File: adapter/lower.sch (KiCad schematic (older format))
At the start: 13 parts, among them J1 MALE, J2 FEMALE, J3 STANDOFF, J4 STANDOFF, J5 STANDOFF, J6 USB_C_Receptacle_USB2.0, J7 DTR, U1 FT232RL

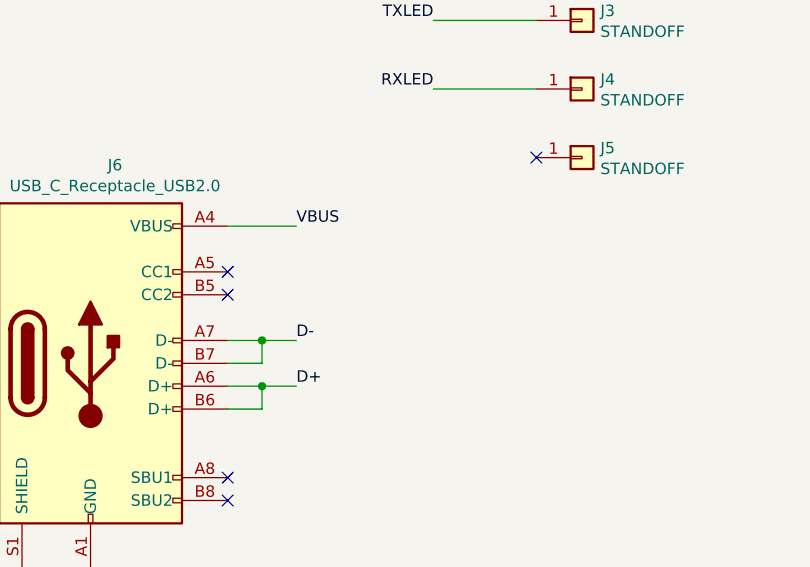
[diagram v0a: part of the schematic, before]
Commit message: Add 56k pullups to fake USB host signature
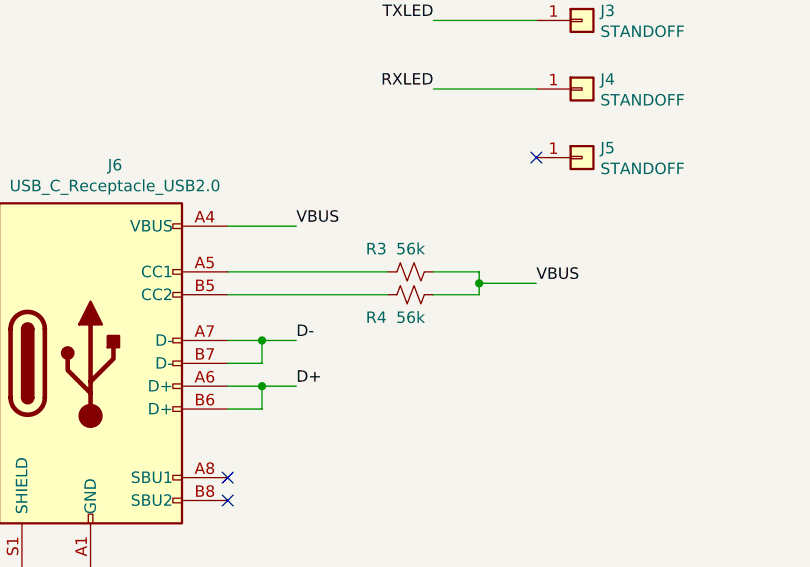
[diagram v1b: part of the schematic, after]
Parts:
- added R3, R4: 56k, symbol Device:R_Small_US
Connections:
- net VBUS: now also R3.1, R4.1
- net at J6.A5 (CC1): now also R3.2
- net at J6.B5 (CC2): now also R4.2
- no-connect marks 16 -> 14
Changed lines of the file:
@@
 	1    0    0    -1
 $EndComp
-NoConn ~ 2150 4100
-NoConn ~ 2150 4200
 NoConn ~ 2150 5000
 NoConn ~ 2150 5100
@@
 $EndComp
 $Comp
-L node:+5VB #PWR?
+L node:+5VB #PWR04
 U 1 1 5FBBDFD6
 P 2550 1100
-F 0 "#PWR?" H 2550 950 50  0001 C CNN
+F 0 "#PWR04" H 2550 950 50  0001 C CNN
 F 1 "+5VB" H 2565 1273 50  0000 C CNN
 F 2 "" H 2550 1100 50  0001 C CNN
@@
 	1200 2200 1200 2450
 $Comp
-L node:+5VB #PWR?
+L node:+5VB #PWR01
 U 1 1 5FBC099F
 P 1200 2200
-F 0 "#PWR?" H 1200 2050 50  0001 C CNN
+F 0 "#PWR01" H 1200 2050 50  0001 C CNN
 F 1 "+5VB" H 1215 2373 50  0000 C CNN
 F 2 "" H 1200 2200 50  0001 C CNN
@@
 $EndComp
 $Comp
-L node:+5VB #PWR?
+L node:+5VB #PWR09
 U 1 1 5FBC0B3A
 P 9000 2000
-F 0 "#PWR?" H 9000 1850 50  0001 C CNN
+F 0 "#PWR09" H 9000 1850 50  0001 C CNN
 F 1 "+5VB" H 9015 2173 50  0000 C CNN
 F 2 "" H 9000 2000 50  0001 C CNN
@@
 $EndComp
 $Comp
-L node:GNDB #PWR?
+L node:GNDB #PWR02
 U 1 1 5FBC113D
 P 1550 5600
-F 0 "#PWR?" H 1550 5350 50  0001 C CNN
+F 0 "#PWR02" H 1550 5350 50  0001 C CNN
 F 1 "GNDB" H 1555 5427 50  0000 C CNN
 F 2 "" H 1550 5600 50  0001 C CNN
@@
 $EndComp
 $Comp
-L node:GNDB #PWR?
+L node:GNDB #PWR03
 U 1 1 5FBC146F
 P 1650 2450
-F 0 "#PWR?" H 1650 2200 50  0001 C CNN
+F 0 "#PWR03" H 1650 2200 50  0001 C CNN
 F 1 "GNDB" H 1655 2277 50  0000 C CNN
 F 2 "" H 1650 2450 50  0001 C CNN
@@
 $EndComp
 $Comp
-L node:GNDB #PWR?
+L node:GNDB #PWR08
 U 1 1 5FBC158B
 P 7850 4900
-F 0 "#PWR?" H 7850 4650 50  0001 C CNN
+F 0 "#PWR08" H 7850 4650 50  0001 C CNN
 F 1 "GNDB" H 8050 4850 50  0000 C CNN
 F 2 "" H 7850 4900 50  0001 C CNN
@@
 $EndComp
 $Comp
-L node:GNDB #PWR?
+L node:GNDB #PWR010
 U 1 1 5FBC1AD4
 P 9000 2700
-F 0 "#PWR?" H 9000 2450 50  0001 C CNN
+F 0 "#PWR010" H 9000 2450 50  0001 C CNN
 F 1 "GNDB" H 9200 2650 50  0000 C CNN
 F 2 "" H 9000 2700 50  0001 C CNN
@@
 $EndComp
 $Comp
-L node:GNDB #PWR?
+L node:GNDB #PWR06
 U 1 1 5FBC1BF2
 P 6000 2650
-F 0 "#PWR?" H 6000 2400 50  0001 C CNN
+F 0 "#PWR06" H 6000 2400 50  0001 C CNN
 F 1 "GNDB" H 6200 2600 50  0000 C CNN
 F 2 "" H 6000 2650 50  0001 C CNN
@@
 $EndComp
 $Comp
-L node:GNDB #PWR?
+L node:GNDB #PWR07
 U 1 1 5FBC1D04
 P 6650 3050
-F 0 "#PWR?" H 6650 2800 50  0001 C CNN
+F 0 "#PWR07" H 6650 2800 50  0001 C CNN
 F 1 "GNDB" H 6450 3000 50  0000 C CNN
 F 2 "" H 6650 3050 50  0001 C CNN
@@
 $EndComp
 $Comp
-L node:GNDB #PWR?
+L node:GNDB #PWR05
 U 1 1 5FBC21C4
 P 3750 1800
-F 0 "#PWR?" H 3750 1550 50  0001 C CNN
+F 0 "#PWR05" H 3750 1550 50  0001 C CNN
 F 1 "GNDB" H 3755 1627 50  0000 C CNN
 F 2 "" H 3750 1800 50  0001 C CNN
@@
 	1    0    0    -1
 $EndComp
+$Comp
+L Device:R_Small_US R3
+U 1 1 5FBF7BD1
+P 2950 4100
+F 0 "R3" V 2850 3950 50  0000 C CNN
+F 1 "56k" V 2850 4100 50  0000 C CNN
+F 2 "" H 2950 4100 50  0001 C CNN
+F 3 "~" H 2950 4100 50  0001 C CNN
+	1    2950 4100
+	0    1    1    0
+$EndComp
+$Comp
+L Device:R_Small_US R4
+U 1 1 5FBF7F1F
+P 2950 4200
+F 0 "R4" V 3050 4050 50  0000 C CNN
+F 1 "56k" V 3050 4200 50  0000 C CNN
+F 2 "" H 2950 4200 50  0001 C CNN
+F 3 "~" H 2950 4200 50  0001 C CNN
+	1    2950 4200
+	0    1    1    0
+$EndComp
+Wire Wire Line
+	2150 4100 2850 4100
+Wire Wire Line
+	2150 4200 2850 4200
+Wire Wire Line
+	3050 4100 3250 4100
+Wire Wire Line
+	3250 4100 3250 4150
+Wire Wire Line
+	3250 4200 3050 4200
+Wire Wire Line
+	3500 4150 3250 4150
+Connection ~ 3250 4150
+Wire Wire Line
+	3250 4150 3250 4200
+Text Label 3500 4150 0    50   ~ 0
+VBUS
 $EndSCHEMATC

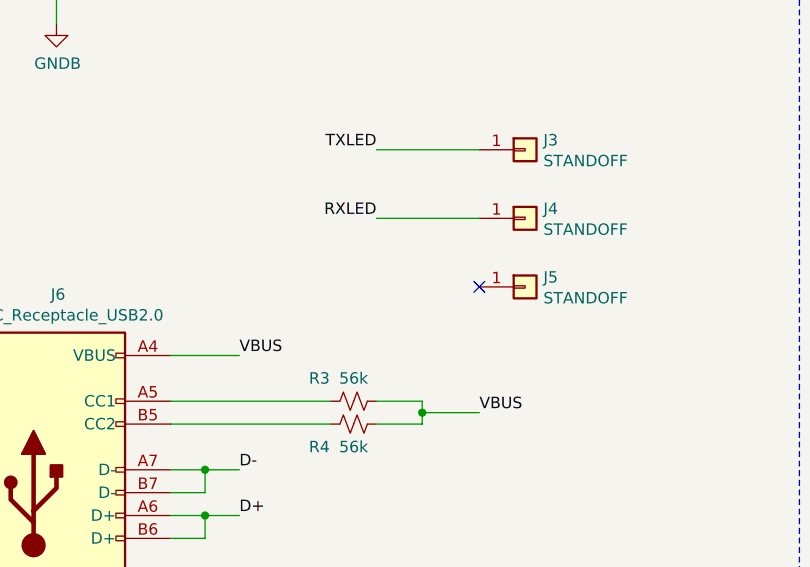
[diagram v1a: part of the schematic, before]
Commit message: Put +5V on standoff: Make LEDs work w/o connection
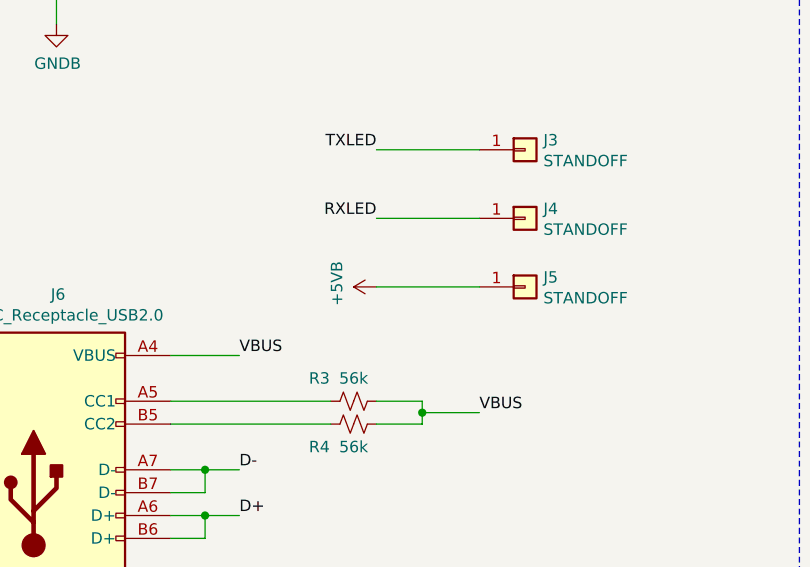
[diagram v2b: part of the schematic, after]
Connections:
- net +5VB: now also J5.1 (Pin_1)
- no-connect marks 14 -> 13
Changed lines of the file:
@@
 	1    0    0    -1
 $EndComp
-NoConn ~ 3500 3600
 $Comp
 L Connector_Generic:Conn_01x01 J4
@@
 Text Label 3500 4150 0    50   ~ 0
 VBUS
+$Comp
+L node:+5VB #PWR?
+U 1 1 5FC06065
+P 3050 3600
+F 0 "#PWR?" H 3050 3450 50  0001 C CNN
+F 1 "+5VB" H 3065 3773 50  0000 C CNN
+F 2 "" H 3050 3600 50  0001 C CNN
+F 3 "" H 3050 3600 50  0001 C CNN
+	1    3050 3600
+	0    -1   -1   0
+$EndComp
+Wire Wire Line
+	3050 3600 3500 3600
 $EndSCHEMATC

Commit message: Assign footprints to pullups
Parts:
- R3, R4: footprint (none) -> Resistor_SMD:R_0805_2012Metric_Pad1.20x1.40mm_HandSolder
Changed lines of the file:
@@
-$EndComp
-$Comp
-L Device:R_Small_US R3
-U 1 1 5FBF7BD1
-P 2950 4100
-F 0 "R3" V 2850 3950 50  0000 C CNN
-F 1 "56k" V 2850 4100 50  0000 C CNN
-F 2 "" H 2950 4100 50  0001 C CNN
-F 3 "~" H 2950 4100 50  0001 C CNN
-	1    2950 4100
-	0    1    1    0
 $EndComp
 $Comp
@@
 F 0 "R4" V 3050 4050 50  0000 C CNN
 F 1 "56k" V 3050 4200 50  0000 C CNN
-F 2 "" H 2950 4200 50  0001 C CNN
+F 2 "Resistor_SMD:R_0805_2012Metric_Pad1.20x1.40mm_HandSolder" H 2950 4200 50  0001 C CNN
 F 3 "~" H 2950 4200 50  0001 C CNN
 	1    2950 4200
@@
 	3050 4100 3250 4100
 Wire Wire Line
-	3250 4100 3250 4150
-Wire Wire Line
 	3250 4200 3050 4200
 Wire Wire Line
 	3500 4150 3250 4150
-Connection ~ 3250 4150
+Wire Wire Line
+	3250 4100 3250 4150
 Wire Wire Line
 	3250 4150 3250 4200
+Connection ~ 3250 4150
 Text Label 3500 4150 0    50   ~ 0
 VBUS
 $Comp
+L Device:R_Small_US R3
+U 1 1 5FBF7BD1
+P 2950 4100
+F 0 "R3" V 2850 3950 50  0000 C CNN
+F 1 "56k" V 2850 4100 50  0000 C CNN
+F 2 "Resistor_SMD:R_0805_2012Metric_Pad1.20x1.40mm_HandSolder" H 2950 4100 50  0001 C CNN
+F 3 "~" H 2950 4100 50  0001 C CNN
+	1    2950 4100
+	0    1    1    0
+$EndComp
+$Comp
 L node:+5VB #PWR0101

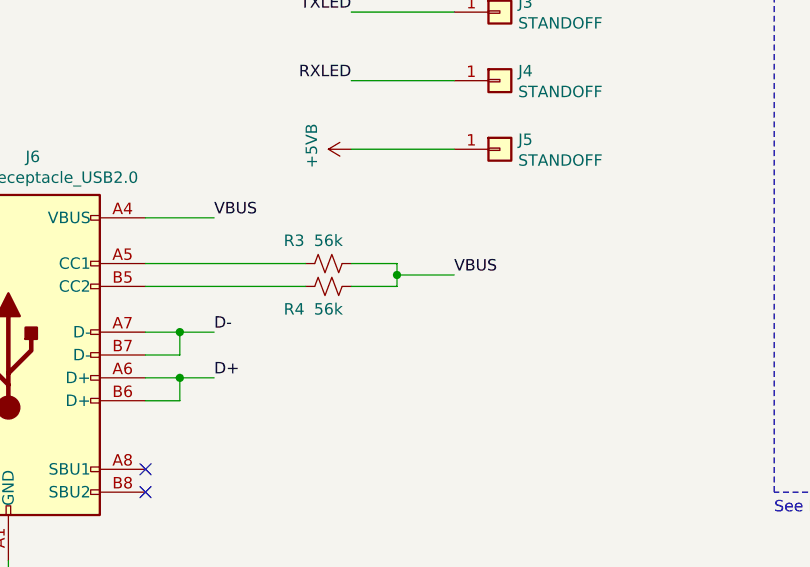
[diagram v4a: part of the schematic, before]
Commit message: Fix: Adapter identif. as down- instead of upstream
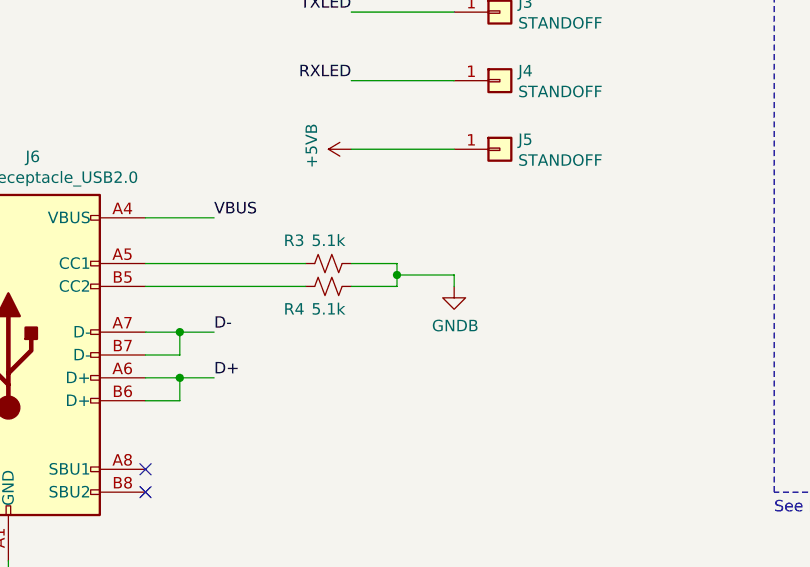
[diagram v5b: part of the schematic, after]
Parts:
- R3, R4: value 56k -> 5.1k
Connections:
- net GNDB: now also R3.1, R4.1
- net VBUS: no longer R3.1, R4.1
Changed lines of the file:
@@
 P 2950 4200
 F 0 "R4" V 3050 4050 50  0000 C CNN
-F 1 "56k" V 3050 4200 50  0000 C CNN
+F 1 "5.1k" V 3050 4200 50  0000 C CNN
 F 2 "Resistor_SMD:R_0805_2012Metric_Pad1.20x1.40mm_HandSolder" H 2950 4200 50  0001 C CNN
 F 3 "~" H 2950 4200 50  0001 C CNN
@@
 	3250 4150 3250 4200
 Connection ~ 3250 4150
-Text Label 3500 4150 0    50   ~ 0
-VBUS
 $Comp
 L Device:R_Small_US R3
@@
 P 2950 4100
 F 0 "R3" V 2850 3950 50  0000 C CNN
-F 1 "56k" V 2850 4100 50  0000 C CNN
+F 1 "5.1k" V 2850 4100 50  0000 C CNN
 F 2 "Resistor_SMD:R_0805_2012Metric_Pad1.20x1.40mm_HandSolder" H 2950 4100 50  0001 C CNN
 F 3 "~" H 2950 4100 50  0001 C CNN
@@
 Wire Wire Line
 	3050 3600 3500 3600
+$Comp
+L node:GNDB #PWR?
+U 1 1 5FCA171C
+P 3500 4200
+F 0 "#PWR?" H 3500 3950 50  0001 C CNN
+F 1 "GNDB" H 3505 4027 50  0000 C CNN
+F 2 "" H 3500 4200 50  0001 C CNN
+F 3 "" H 3500 4200 50  0001 C CNN
+	1    3500 4200
+	1    0    0    -1
+$EndComp
+Wire Wire Line
+	3500 4200 3500 4150
 $EndSCHEMATC

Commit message: No change
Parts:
- R3, R4: value 5.1k -> 56k
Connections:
- net GNDB: no longer R3.1, R4.1
- net VBUS: now also R3.1, R4.1

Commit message: Fix pinout
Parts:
- removed J1: MALE, Connector_PinHeader_2.54mm:PinHeader_2x02_P2.54mm_Horizontal, symbol Connector_Generic:Conn_02x02_Top_Bottom
- J2: symbol Connector_Generic:Conn_02x02_Odd_Even -> Connector_Generic:Conn_02x02_Top_Bottom
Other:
- moved on the sheet: J2
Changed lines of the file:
@@
 	0    1    1    0
 $EndComp
-$Comp
-L Connector_Generic:Conn_02x02_Odd_Even J?
-U 1 1 5FA83015
-P 3100 1650
-AR Path="/5FA83015" Ref="J?"  Part="1"
-AR Path="/5FA6C89B/5FA83015" Ref="J2"  Part="1"
-F 0 "J2" H 3150 1867 50  0000 C CNN
-F 1 "FEMALE" H 3150 1776 50  0000 C CNN
-F 2 "Connector_PinSocket_2.54mm:PinSocket_2x02_P2.54mm_Horizontal" H 3100 1650 50  0001 C CNN
-F 3 "~" H 3100 1650 50  0001 C CNN
-	1    3100 1650
-	1    0    0    -1
-$EndComp
-Wire Wire Line
-	3400 1650 3500 1650
-Wire Wire Line
-	2550 1750 2900 1750
-Wire Wire Line
-	2800 1650 2900 1650
 Wire Wire Line
 	3050 3000 3500 3000
@@
 	3050 3600 3500 3600
 $Comp
-L node:+5VB #PWR04
-U 1 1 5FBBDFD6
-P 2550 1100
-F 0 "#PWR04" H 2550 950 50  0001 C CNN
-F 1 "+5VB" H 2565 1273 50  0000 C CNN
-F 2 "" H 2550 1100 50  0001 C CNN
-F 3 "" H 2550 1100 50  0001 C CNN
-	1    2550 1100
-	1    0    0    -1
-$EndComp
-Wire Wire Line
-	3750 1750 3750 1800
-Wire Wire Line
-	2800 1250 2800 1650
-Wire Wire Line
-	2900 1250 2800 1250
-Connection ~ 3750 1750
-Wire Wire Line
-	3750 1150 3750 1750
-Wire Wire Line
-	3400 1150 3750 1150
-Wire Wire Line
-	3500 1250 3500 1650
-Wire Wire Line
-	3400 1250 3500 1250
-Wire Wire Line
-	2550 1100 2550 1150
-Wire Wire Line
-	2550 1150 2550 1750
-Connection ~ 2550 1150
-Wire Wire Line
-	2900 1150 2550 1150
-$Comp
-L Connector_Generic:Conn_02x02_Top_Bottom J?
-U 1 1 5FA6D1B6
-P 3100 1150
-AR Path="/5FA6D1B6" Ref="J?"  Part="1"
-AR Path="/5FA6C89B/5FA6D1B6" Ref="J1"  Part="1"
-F 0 "J1" H 3150 1367 50  0000 C CNN
-F 1 "MALE" H 3150 1276 50  0000 C CNN
-F 2 "Connector_PinHeader_2.54mm:PinHeader_2x02_P2.54mm_Horizontal" H 3100 1150 50  0001 C CNN
-F 3 "~" H 3100 1150 50  0001 C CNN
-	1    3100 1150
-	1    0    0    -1
-$EndComp
-Wire Wire Line
-	3400 1750 3750 1750
-$Comp
-L node:GNDB #PWR05
-U 1 1 5FBC21C4
-P 3750 1800
-F 0 "#PWR05" H 3750 1550 50  0001 C CNN
-F 1 "GNDB" H 3755 1627 50  0000 C CNN
-F 2 "" H 3750 1800 50  0001 C CNN
-F 3 "" H 3750 1800 50  0001 C CNN
-	1    3750 1800
-	1    0    0    -1
-$EndComp
-Text Label 2800 1250 2    50   ~ 0
-RXD
-Text Label 3500 1250 0    50   ~ 0
-TXD
-$Comp
 L Device:R_Small_US R4
 U 1 1 5FBF7F1F
@@
 Text Label 3500 4150 0    50   ~ 0
 VBUS
+Text Label 3050 1650 2    50   ~ 0
+RXD
+Text Label 3050 1750 2    50   ~ 0
+TXD
+Wire Wire Line
+	3150 1650 3050 1650
+Wire Wire Line
+	3150 1750 3050 1750
+Wire Wire Line
+	3750 1750 3750 1800
+Wire Wire Line
+	3650 1750 3750 1750
+Wire Wire Line
+	3750 1650 3750 1600
+Wire Wire Line
+	3650 1650 3750 1650
+$Comp
+L node:+5VB #PWR?
+U 1 1 5FD11CF7
+P 3750 1600
+F 0 "#PWR?" H 3750 1450 50  0001 C CNN
+F 1 "+5VB" H 3765 1773 50  0000 C CNN
+F 2 "" H 3750 1600 50  0001 C CNN
+F 3 "" H 3750 1600 50  0001 C CNN
+	1    3750 1600
+	1    0    0    -1
+$EndComp
+$Comp
+L node:GNDB #PWR?
+U 1 1 5FD11BCA
+P 3750 1800
+F 0 "#PWR?" H 3750 1550 50  0001 C CNN
+F 1 "GNDB" H 3755 1627 50  0000 C CNN
+F 2 "" H 3750 1800 50  0001 C CNN
+F 3 "" H 3750 1800 50  0001 C CNN
+	1    3750 1800
+	1    0    0    -1
+$EndComp
+$Comp
+L Connector_Generic:Conn_02x02_Top_Bottom J?
+U 1 1 5FA83015
+P 3350 1650
+AR Path="/5FA83015" Ref="J?"  Part="1"
+AR Path="/5FA6C89B/5FA83015" Ref="J2"  Part="1"
+F 0 "J2" H 3400 1867 50  0000 C CNN
+F 1 "FEMALE" H 3400 1776 50  0000 C CNN
+F 2 "Connector_PinSocket_2.54mm:PinSocket_2x02_P2.54mm_Horizontal" H 3350 1650 50  0001 C CNN
+F 3 "~" H 3350 1650 50  0001 C CNN
+	1    3350 1650
+	1    0    0    -1
+$EndComp
 $EndSCHEMATC

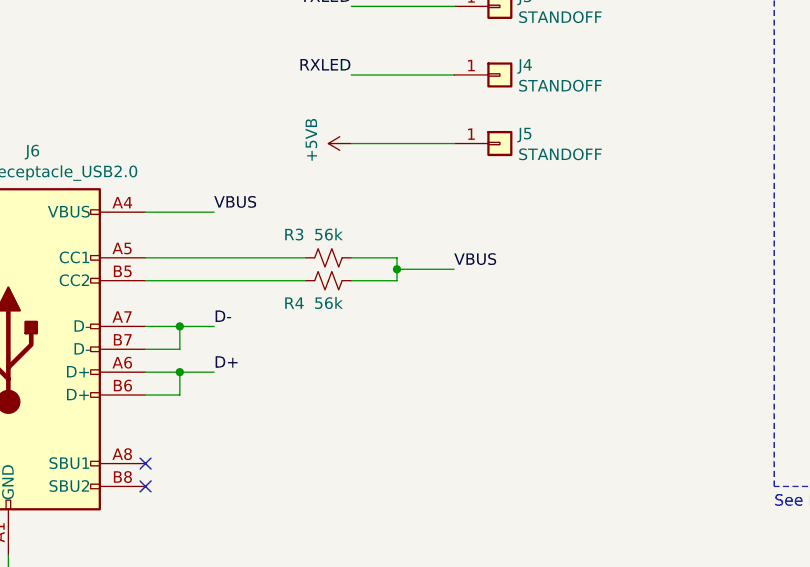
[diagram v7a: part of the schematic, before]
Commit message: Fix: USB-C port no configured as downstream
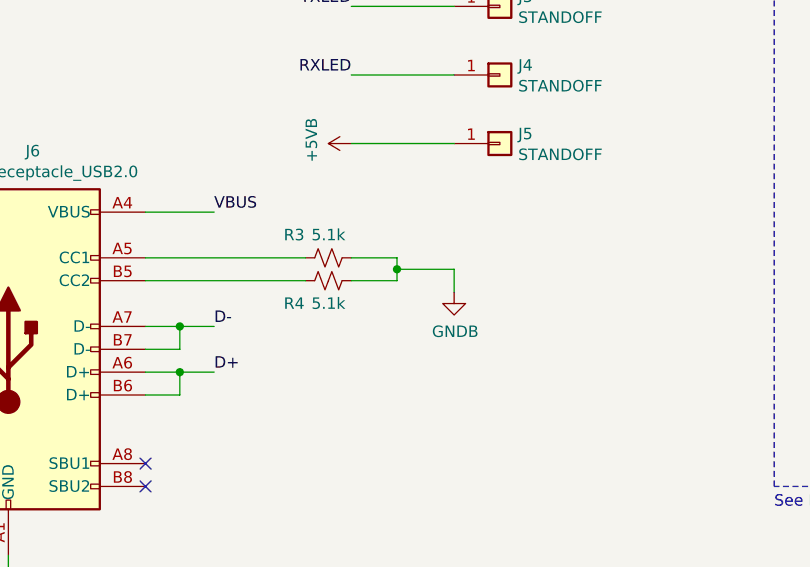
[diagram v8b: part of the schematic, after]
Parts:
- R3, R4: value 56k -> 5.1k
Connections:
- net GNDB: now also R3.1, R4.1
- net VBUS: no longer R3.1, R4.1
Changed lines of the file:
@@
 P 2950 4200
 F 0 "R4" V 3050 4050 50  0000 C CNN
-F 1 "56k" V 3050 4200 50  0000 C CNN
+F 1 "5.1k" V 3050 4200 50  0000 C CNN
 F 2 "Resistor_SMD:R_0805_2012Metric_Pad1.20x1.40mm_HandSolder" H 2950 4200 50  0001 C CNN
 F 3 "~" H 2950 4200 50  0001 C CNN
@@
 P 2950 4100
 F 0 "R3" V 2850 3950 50  0000 C CNN
-F 1 "56k" V 2850 4100 50  0000 C CNN
+F 1 "5.1k" V 2850 4100 50  0000 C CNN
 F 2 "Resistor_SMD:R_0805_2012Metric_Pad1.20x1.40mm_HandSolder" H 2950 4100 50  0001 C CNN
 F 3 "~" H 2950 4100 50  0001 C CNN
@@
 	0    1    1    0
 $EndComp
-Text Label 3500 4150 0    50   ~ 0
-VBUS
 Text Label 3050 1650 2    50   ~ 0
 RXD
@@
 	1    0    0    -1
 $EndComp
+$Comp
+L node:GNDB #PWR?
+U 1 1 5FD33CC5
+P 3500 4250
+F 0 "#PWR?" H 3500 4000 50  0001 C CNN
+F 1 "GNDB" H 3505 4077 50  0000 C CNN
+F 2 "" H 3500 4250 50  0001 C CNN
+F 3 "" H 3500 4250 50  0001 C CNN
+	1    3500 4250
+	1    0    0    -1
+$EndComp
+Wire Wire Line
+	3500 4150 3500 4250
 $EndSCHEMATC
